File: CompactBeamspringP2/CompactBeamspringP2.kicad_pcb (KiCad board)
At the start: 2 copper layers, 162.3 x 33.2 mm, 54 parts, among them J1 BEAMSPRING CONNECTOR, J3 EXPANSION HEADER, U1 MCP4921-E, U2 LM339A, U3 74AHC595, U4 74AHC595, U5 ProMicro, U7 74AHC595

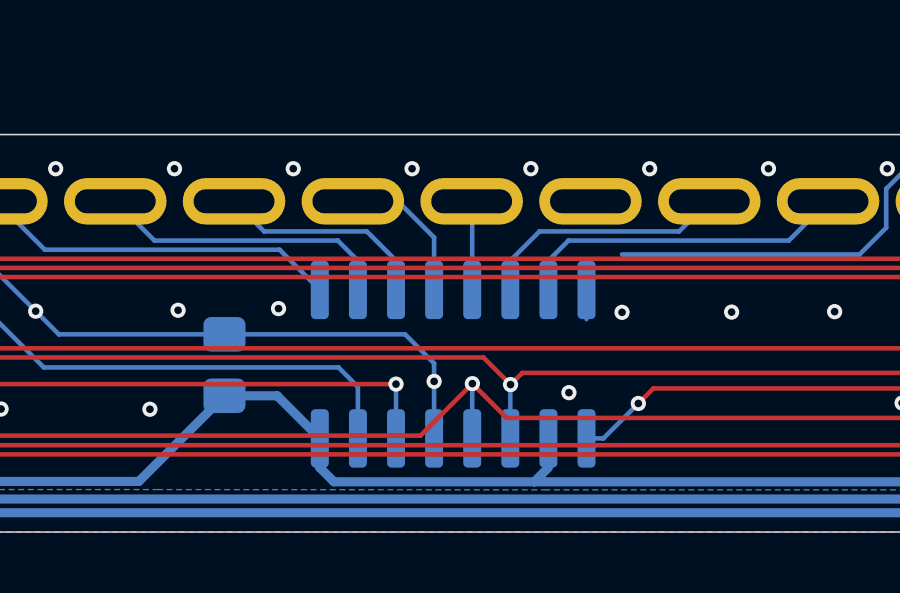
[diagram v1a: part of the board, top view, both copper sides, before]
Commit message: 2-panel: added silkscreen for jlcpcb part number. 1-panel already has it
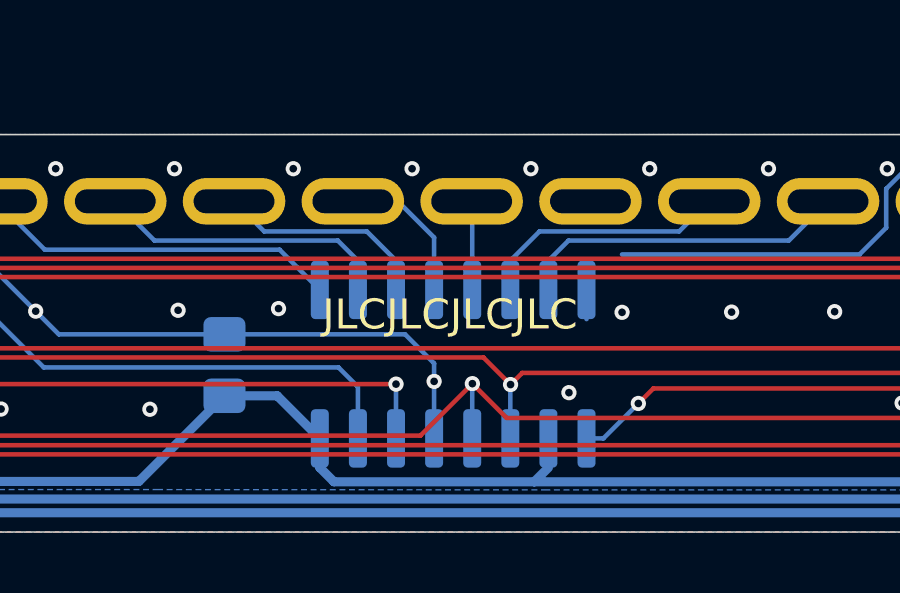
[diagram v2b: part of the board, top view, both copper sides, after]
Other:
- board text added: "JLCJLCJLCJLC"
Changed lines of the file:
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@@
   (general
     (thickness 1.6)
-    (drawings 55)
+    (drawings 56)
     (tracks 1218)
     (zones 0)
@@
     (solder_mask_min_width 0.101)
     (aux_axis_origin 108.7 141.35)
-    (visible_elements 7FFFFF7F)
+    (visible_elements 7FFFF77F)
     (pcbplotparams
       (layerselection 0x010fc_ffffffff)
@@
     )
   )
+  (gr_text JLCJLCJLCJLC (at 198.5 134.1) (layer F.SilkS)
+    (effects (font (size 1 1) (thickness 0.15)))
+  )
   (gr_arc (start 266.75 127.5) (end 266.75 128.1) (angle -180) (layer Edge.Cuts) (width 0.05))

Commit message: More mods
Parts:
- removed the C1 at (238.6, 138.5)
- removed the C1 at (141.0, 111.0)
- removed the C2 at (156.2, 135.8)
- removed the C2 at (223.4, 113.7)
- removed the C3 at (260.5, 135.8)
- removed the C3 at (119.1, 113.7)
- removed the C4 at (191.0, 135.8)
- removed the C4 at (188.7, 113.7)
- removed the C5 at (223.5, 135.8)
- removed the C5 at (156.2, 113.7)
- removed the C6 at (247.3, 133.2)
- removed the C6 at (132.4, 116.3)
- removed the H1 at (269.1, 139.5)
- removed the H1 at (110.5, 110.0)
- removed the J1 at (201.2, 130.3)
- removed the J1 at (178.4, 119.2)
- removed the J3 at (143.4, 127.0)
- removed the J3 at (236.3, 122.5)
- removed the NT1 at (116.4, 135.6)
- removed the NT1 at (263.3, 113.9)
- removed the NT2 at (117.5, 126.5)
- removed the NT2 at (262.2, 123.0)
- removed the R1 at (266.6, 131.1)
- removed the R1 at (113.1, 118.4)
- removed the R2 at (268.9, 131.1)
- removed the R2 at (110.7, 118.4)
- removed the R3 at (246.0, 136.3)
- removed the R3 at (133.7, 113.2)
- removed the R4 at (242.7, 138.5)
- removed the R4 at (137.0, 111.0)
- removed the R5 at (248.4, 136.7)
- removed the R5 at (131.2, 112.8)
- removed the R6 at (138.9, 128.1)
- removed the R6 at (240.7, 121.4)
- removed the R7 at (138.9, 130.1)
- removed the R7 at (240.7, 119.4)
- removed the REF** at (111.2, 136.7)
- removed the REF** at (265.6, 139.6)
- removed the REF** at (268.4, 112.8)
- removed the REF** at (114.1, 109.9)
- removed the RN1 at (262.9, 131.1)
- removed the RN1 at (116.7, 118.4)
- removed the U1 at (240.9, 134.6)
- removed the U1 at (138.8, 114.9)
- removed the U2 at (254.5, 136.2)
- removed the U2 at (125.2, 113.3)
- removed the U3 at (164.3, 135.8)
- removed the U3 at (215.4, 113.7)
- removed the U4 at (198.6, 135.8)
- removed the U4 at (181.0, 113.7)
- removed the U5 at (125.0, 131.9)
- removed the U5 at (254.6, 117.6)
- removed the U7 at (230.6, 135.8)
- removed the U7 at (149.0, 113.7)
- added C1: 0U1, Capacitor_SMD:C_0805_2012Metric_Pad1.15x1.40mm_HandSolder, B.Cu at (232.9, 129.5)
- added C1: 0U1, Capacitor_SMD:C_0805_2012Metric_Pad1.15x1.40mm_HandSolder, B.Cu at (135.3, 101.9)
- added C2: 0U1, Capacitor_SMD:C_0805_2012Metric_Pad1.15x1.40mm_HandSolder, B.Cu at (150.5, 126.7)
- added C2: 0U1, Capacitor_SMD:C_0805_2012Metric_Pad1.15x1.40mm_HandSolder, B.Cu at (217.7, 104.7)
- added C3: 0U1, Capacitor_SMD:C_0805_2012Metric_Pad1.15x1.40mm_HandSolder, B.Cu at (254.8, 126.8)
- added C3: 0U1, Capacitor_SMD:C_0805_2012Metric_Pad1.15x1.40mm_HandSolder, B.Cu at (113.4, 104.6)
- added C4: 0U1, Capacitor_SMD:C_0805_2012Metric_Pad1.15x1.40mm_HandSolder, B.Cu at (185.2, 126.7)
- added C4: 0U1, Capacitor_SMD:C_0805_2012Metric_Pad1.15x1.40mm_HandSolder, B.Cu at (182.9, 104.7)
- added C5: 0U1, Capacitor_SMD:C_0805_2012Metric_Pad1.15x1.40mm_HandSolder, B.Cu at (217.7, 126.7)
- added C5: 0U1, Capacitor_SMD:C_0805_2012Metric_Pad1.15x1.40mm_HandSolder, B.Cu at (150.4, 104.7)
- added C6: 0U1, Capacitor_SMD:C_0805_2012Metric_Pad1.15x1.40mm_HandSolder, B.Cu at (241.5, 124.2)
- added C6: 0U1, Capacitor_SMD:C_0805_2012Metric_Pad1.15x1.40mm_HandSolder, B.Cu at (126.6, 107.2)
- added H1: MountingHole_Pad, TH-XWhatsIt:ChassisGnd, B.Cu at (263.4, 130.4)
- added H1: MountingHole_Pad, TH-XWhatsIt:ChassisGnd, B.Cu at (104.8, 101.0)
- added J1: BEAMSPRING CONNECTOR, TH-XWhatsIt:30-pin-universal-beamspring-connector_v2, F.Cu at (195.5, 121.3)
- added J1: BEAMSPRING CONNECTOR, TH-XWhatsIt:30-pin-universal-beamspring-connector_v2, F.Cu at (172.7, 110.1)
- added J2: PadsToShort, TH-XWhatsIt:PadsToShort, B.Cu at (109.0, 118.5)
- added J2: PadsToShort, TH-XWhatsIt:PadsToShort, B.Cu at (259.1, 112.9)
- added J3: EXPANSION HEADER, Connector_PinHeader_2.54mm:PinHeader_2x03_P2.54mm_Vertical, F.Cu at (137.6, 117.9)
- added J3: EXPANSION HEADER, Connector_PinHeader_2.54mm:PinHeader_2x03_P2.54mm_Vertical, F.Cu at (230.5, 113.5)
- added NT1: Net-Tie_3, NetTie:NetTie-3_THT_Pad0.3mm, B.Cu at (110.6, 126.5)
- added NT1: Net-Tie_3, NetTie:NetTie-3_THT_Pad0.3mm, B.Cu at (257.5, 104.9)
- added NT2: Net-Tie_3, NetTie:NetTie-3_THT_Pad0.3mm, B.Cu at (111.7, 117.4)
- added NT2: Net-Tie_3, NetTie:NetTie-3_THT_Pad0.3mm, B.Cu at (256.4, 114.0)
- added R1: 4K7, Resistor_SMD:R_0805_2012Metric_Pad1.15x1.40mm_HandSolder, B.Cu at (260.8, 122.0)
- added R1: 4K7, Resistor_SMD:R_0805_2012Metric_Pad1.15x1.40mm_HandSolder, B.Cu at (107.3, 109.4)
- added R2: 1K, Resistor_SMD:R_0805_2012Metric_Pad1.15x1.40mm_HandSolder, B.Cu at (263.2, 122.0)
- added R2: 1K, Resistor_SMD:R_0805_2012Metric_Pad1.15x1.40mm_HandSolder, B.Cu at (105.0, 109.4)
- added R3: 20K, Resistor_SMD:R_0805_2012Metric_Pad1.15x1.40mm_HandSolder, B.Cu at (240.2, 127.2)
- added R3: 20K, Resistor_SMD:R_0805_2012Metric_Pad1.15x1.40mm_HandSolder, B.Cu at (127.9, 104.2)
- added R4: 20K, Resistor_SMD:R_0805_2012Metric_Pad1.15x1.40mm_HandSolder, B.Cu at (236.9, 129.5)
- added R4: 20K, Resistor_SMD:R_0805_2012Metric_Pad1.15x1.40mm_HandSolder, B.Cu at (131.2, 101.9)
- added R5: 4K7, Resistor_SMD:R_0805_2012Metric_Pad1.15x1.40mm_HandSolder, B.Cu at (242.7, 127.6)
- added R5: 4K7, Resistor_SMD:R_0805_2012Metric_Pad1.15x1.40mm_HandSolder, B.Cu at (125.5, 103.8)
- added R6: Not Mounted, Resistor_SMD:R_0805_2012Metric_Pad1.15x1.40mm_HandSolder, B.Cu at (132.3, 119.0)
- added R6: Not Mounted, Resistor_SMD:R_0805_2012Metric_Pad1.15x1.40mm_HandSolder, B.Cu at (235.8, 112.4)
- added R7: Not Mounted, Resistor_SMD:R_0805_2012Metric_Pad1.15x1.40mm_HandSolder, B.Cu at (132.3, 121.0)
- added R7: Not Mounted, Resistor_SMD:R_0805_2012Metric_Pad1.15x1.40mm_HandSolder, B.Cu at (235.8, 110.4)
- added R8: Not Mounted, Resistor_SMD:R_0805_2012Metric_Pad1.15x1.40mm_HandSolder, B.Cu at (132.3, 123.0)
- added R8: Not Mounted, Resistor_SMD:R_0805_2012Metric_Pad1.15x1.40mm_HandSolder, B.Cu at (235.8, 108.4)
- added REF**: tooling_hole, TH-XWhatsIt:tooling_hole, F.Cu at (105.5, 127.6)
- added REF**: tooling_hole, TH-XWhatsIt:tooling_hole, F.Cu at (259.8, 130.6)
- added REF**: tooling_hole, TH-XWhatsIt:tooling_hole, F.Cu at (262.7, 103.8)
- added REF**: tooling_hole, TH-XWhatsIt:tooling_hole, F.Cu at (108.3, 100.8)
- added RN1: 100K, Resistor_SMD:R_Array_Convex_4x0603, B.Cu at (257.2, 122.1)
- added RN1: 100K, Resistor_SMD:R_Array_Convex_4x0603, B.Cu at (111.0, 109.3)
- added TP1: Dac Output, TestPoint:TestPoint_Pad_D1.0mm, B.Cu at (240.9, 131.1)
- added TP1: Dac Output, TestPoint:TestPoint_Pad_D1.0mm, B.Cu at (127.2, 100.3)
- added TP2: Threshold Voltage, TestPoint:TestPoint_Pad_D1.0mm, B.Cu at (256.8, 129.9)
- added TP2: Threshold Voltage, TestPoint:TestPoint_Pad_D1.0mm, B.Cu at (111.3, 101.5)
- added U1: MCP4921-E, Package_SO:SOIC-8_3.9x4.9mm_P1.27mm, B.Cu at (235.1, 125.6)
- added U1: MCP4921-E, Package_SO:SOIC-8_3.9x4.9mm_P1.27mm, B.Cu at (133.0, 105.8)
- added U2: LM339A, Package_SO:SOIC-14_3.9x8.7mm_P1.27mm, B.Cu at (248.7, 127.1)
- added U2: LM339A, Package_SO:SOIC-14_3.9x8.7mm_P1.27mm, B.Cu at (119.4, 104.3)
- added U3: 74AHC595, Package_SO:SOIC-16_3.9x9.9mm_P1.27mm, B.Cu at (158.5, 126.7)
- added U3: 74AHC595, Package_SO:SOIC-16_3.9x9.9mm_P1.27mm, B.Cu at (209.6, 104.7)
- added U4: 74AHC595, Package_SO:SOIC-16_3.9x9.9mm_P1.27mm, B.Cu at (192.9, 126.7)
- added U4: 74AHC595, Package_SO:SOIC-16_3.9x9.9mm_P1.27mm, B.Cu at (175.3, 104.7)
- added U5: ProMicro, promicro:ProMicro, F.Cu at (119.3, 122.8)
- added U5: ProMicro, promicro:ProMicro, F.Cu at (248.9, 108.6)
- added U7: 74AHC595, Package_SO:SOIC-16_3.9x9.9mm_P1.27mm, B.Cu at (224.9, 126.7)
- added U7: 74AHC595, Package_SO:SOIC-16_3.9x9.9mm_P1.27mm, B.Cu at (143.3, 104.7)
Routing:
- net HEADER3: track 41.2 -> 89.9 mm
- net GNDD: track 267.9 -> 221.8 mm, vias 126 -> 146
- net GND: track 0.00 -> 44.3 mm
- net Net-(NT1-Pad2): track 42.9 -> 0.00 mm
- net GNDA: track 305.2 -> 262.6 mm, vias 52 -> 64
- net HEADER4: track 51.4 -> 87.2 mm
- net Net-(R8-Pad1): track 0.00 -> 30.3 mm
- net ROW1: track 239.3 -> 265.6 mm
- net HEADER2: track 90.4 -> 66.9 mm, vias 0 -> 4
- net +5VD: track 296.1 -> 317.2 mm
- net HEADER1: track 108.4 -> 87.8 mm, vias 0 -> 4
- net +5VA: track 373.7 -> 393.7 mm, vias 0 -> 4
- net ROW3: track 236.3 -> 255.7 mm
- net RST: track 0.00 -> 12.7 mm
- net Net-(R4-Pad2): track 5.33 -> 18.0 mm
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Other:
- outline, holes or cut-outs redrawn
- board text added: "Compact-Beamspring Rev1.2"
- board text added: "DAC"
- board text added: "Threshold"
- board text added: "Voltage"
- board text added: "Vout"
- board text removed: "Compact-Beamspring Rev1.1"
- board text removed: "JLCJLCJLCJLC"

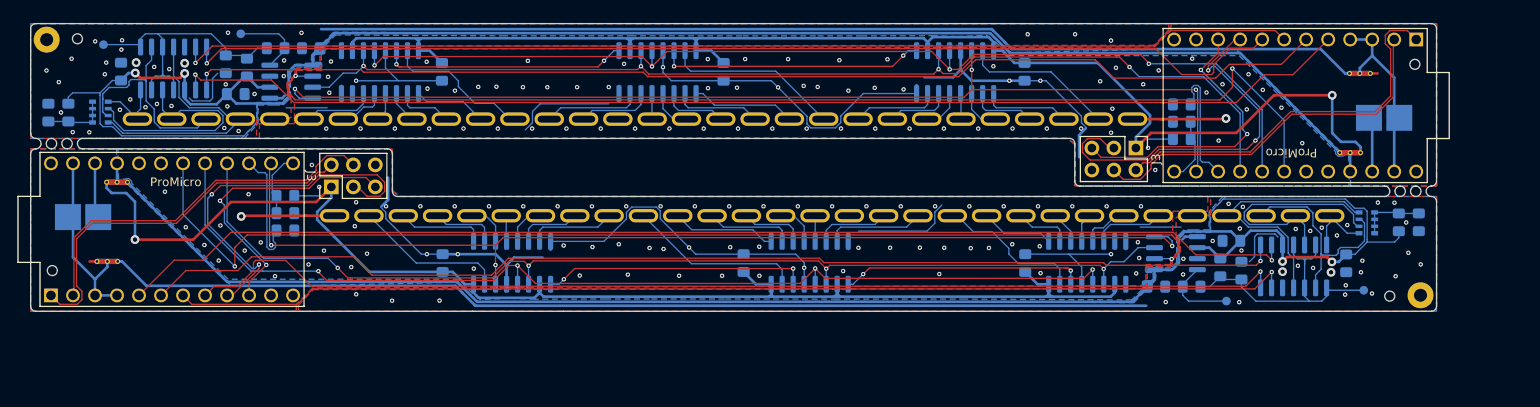
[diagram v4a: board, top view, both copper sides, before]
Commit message: Moved to individual resistors instead of resistor network, added a bit more space next to the promicro
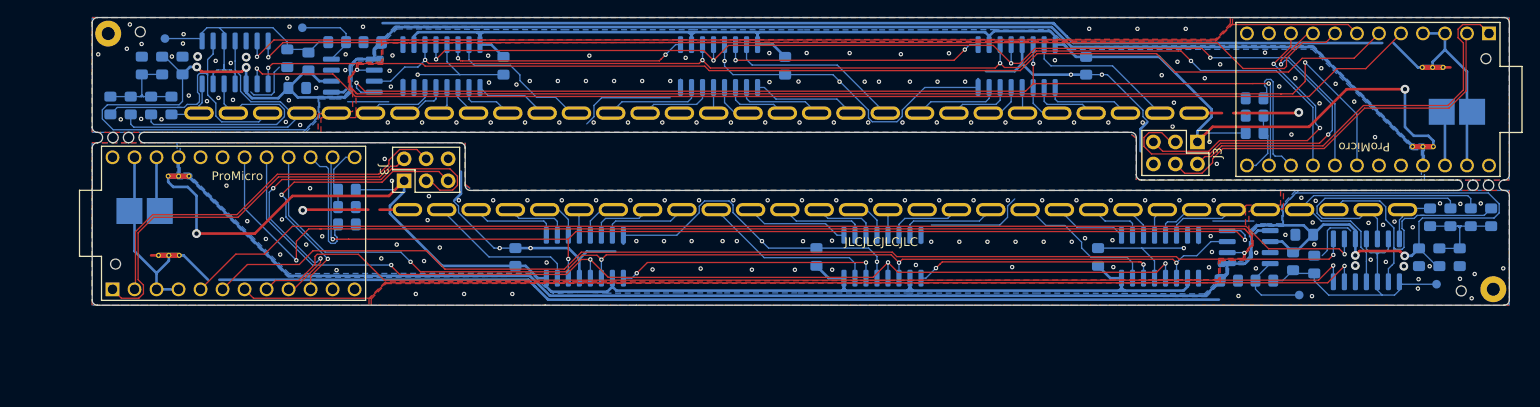
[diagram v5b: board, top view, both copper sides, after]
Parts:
- removed the C1 at (232.9, 129.5)
- removed the C1 at (135.3, 101.9)
- removed the C2 at (150.5, 126.7)
- removed the C2 at (217.7, 104.7)
- removed the C3 at (254.8, 126.8)
- removed the C3 at (113.4, 104.6)
- removed the C4 at (185.2, 126.7)
- removed the C4 at (182.9, 104.7)
- removed the C5 at (217.7, 126.7)
- removed the C5 at (150.4, 104.7)
- removed the C6 at (241.5, 124.2)
- removed the C6 at (126.6, 107.2)
- removed the H1 at (263.4, 130.4)
- removed the H1 at (104.8, 101.0)
- removed the J1 at (195.5, 121.3)
- removed the J1 at (172.7, 110.1)
- removed the J2 at (109.0, 118.5)
- removed the J2 at (259.1, 112.9)
- removed the J3 at (137.6, 117.9)
- removed the J3 at (230.5, 113.5)
- removed the NT1 at (110.6, 126.5)
- removed the NT1 at (257.5, 104.9)
- removed the NT2 at (111.7, 117.4)
- removed the NT2 at (256.4, 114.0)
- removed the R1 at (260.8, 122.0)
- removed the R1 at (107.3, 109.4)
- removed the R2 at (263.2, 122.0)
- removed the R2 at (105.0, 109.4)
- removed the R3 at (240.2, 127.2)
- removed the R3 at (127.9, 104.2)
- removed the R4 at (236.9, 129.5)
- removed the R4 at (131.2, 101.9)
- removed the R5 at (242.7, 127.6)
- removed the R5 at (125.5, 103.8)
- removed the R6 at (132.3, 119.0)
- removed the R6 at (235.8, 112.4)
- removed the R7 at (132.3, 121.0)
- removed the R7 at (235.8, 110.4)
- removed the R8 at (132.3, 123.0)
- removed the R8 at (235.8, 108.4)
- removed the REF** at (105.5, 127.6)
- removed the REF** at (259.8, 130.6)
- removed the REF** at (262.7, 103.8)
- removed the REF** at (108.3, 100.8)
- removed RN1 (x2): 100K, Resistor_SMD:R_Array_Convex_4x0603
- removed the TP1 at (240.9, 131.1)
- removed the TP1 at (127.2, 100.3)
- removed the TP2 at (256.8, 129.9)
- removed the TP2 at (111.3, 101.5)
- removed the U1 at (235.1, 125.6)
- removed the U1 at (133.0, 105.8)
- removed the U2 at (248.7, 127.1)
- removed the U2 at (119.4, 104.3)
- removed the U3 at (158.5, 126.7)
- removed the U3 at (209.6, 104.7)
- removed the U4 at (192.9, 126.7)
- removed the U4 at (175.3, 104.7)
- removed the U5 at (119.3, 122.8)
- removed the U5 at (248.9, 108.6)
- removed the U7 at (224.9, 126.7)
- removed the U7 at (143.3, 104.7)
- added C1: 0U1, Capacitor_SMD:C_0805_2012Metric_Pad1.15x1.40mm_HandSolder, B.Cu at (241.3, 128.8)
- added C1: 0U1, Capacitor_SMD:C_0805_2012Metric_Pad1.15x1.40mm_HandSolder, B.Cu at (142.4, 101.2)
- added C2: 0U1, Capacitor_SMD:C_0805_2012Metric_Pad1.15x1.40mm_HandSolder, B.Cu at (158.9, 126.0)
- added C2: 0U1, Capacitor_SMD:C_0805_2012Metric_Pad1.15x1.40mm_HandSolder, B.Cu at (224.8, 104.0)
- added C3: 0U1, Capacitor_SMD:C_0805_2012Metric_Pad1.15x1.40mm_HandSolder, B.Cu at (263.2, 126.1)
- added C3: 0U1, Capacitor_SMD:C_0805_2012Metric_Pad1.15x1.40mm_HandSolder, B.Cu at (120.5, 103.9)
- added C4: 0U1, Capacitor_SMD:C_0805_2012Metric_Pad1.15x1.40mm_HandSolder, B.Cu at (193.6, 126.0)
- added C4: 0U1, Capacitor_SMD:C_0805_2012Metric_Pad1.15x1.40mm_HandSolder, B.Cu at (190.0, 104.0)
- added C5: 0U1, Capacitor_SMD:C_0805_2012Metric_Pad1.15x1.40mm_HandSolder, B.Cu at (226.1, 126.0)
- added C5: 0U1, Capacitor_SMD:C_0805_2012Metric_Pad1.15x1.40mm_HandSolder, B.Cu at (157.5, 104.0)
- added C6: 0U1, Capacitor_SMD:C_0805_2012Metric_Pad1.15x1.40mm_HandSolder, B.Cu at (249.9, 123.5)
- added C6: 0U1, Capacitor_SMD:C_0805_2012Metric_Pad1.15x1.40mm_HandSolder, B.Cu at (133.7, 106.5)
- added H1: MountingHole_Pad, TH-XWhatsIt:ChassisGnd, B.Cu at (271.8, 129.8)
- added H1: MountingHole_Pad, TH-XWhatsIt:ChassisGnd, B.Cu at (111.9, 100.2)
- added J1: BEAMSPRING CONNECTOR, TH-XWhatsIt:30-pin-universal-beamspring-connector_v2, F.Cu at (203.9, 120.6)
- added J1: BEAMSPRING CONNECTOR, TH-XWhatsIt:30-pin-universal-beamspring-connector_v2, F.Cu at (179.8, 109.4)
- added J2: PadsToShort, TH-XWhatsIt:PadsToShort, B.Cu at (116.1, 117.8)
- added J2: PadsToShort, TH-XWhatsIt:PadsToShort, B.Cu at (267.6, 112.2)
- added J3: EXPANSION HEADER, Connector_PinHeader_2.54mm:PinHeader_2x03_P2.54mm_Vertical, F.Cu at (146.0, 117.2)
- added J3: EXPANSION HEADER, Connector_PinHeader_2.54mm:PinHeader_2x03_P2.54mm_Vertical, F.Cu at (237.6, 112.8)
- added NT1: Net-Tie_3, NetTie:NetTie-3_THT_Pad0.3mm, B.Cu at (117.7, 125.8)
- added NT1: Net-Tie_3, NetTie:NetTie-3_THT_Pad0.3mm, B.Cu at (265.9, 104.2)
- added NT2: Net-Tie_3, NetTie:NetTie-3_THT_Pad0.3mm, B.Cu at (118.8, 116.7)
- added NT2: Net-Tie_3, NetTie:NetTie-3_THT_Pad0.3mm, B.Cu at (264.8, 113.3)
- added R1: 4K7, Resistor_SMD:R_0805_2012Metric_Pad1.15x1.40mm_HandSolder, B.Cu at (265.5, 126.1)
- added R1: 4K7, Resistor_SMD:R_0805_2012Metric_Pad1.15x1.40mm_HandSolder, B.Cu at (118.1, 103.9)
- added R10: 100k 1%, Resistor_SMD:R_0805_2012Metric_Pad1.15x1.40mm_HandSolder, B.Cu at (264.4, 121.5)
- added R10: 100k 1%, Resistor_SMD:R_0805_2012Metric_Pad1.15x1.40mm_HandSolder, B.Cu at (119.2, 108.5)
- added R11: 100k 1%, Resistor_SMD:R_0805_2012Metric_Pad1.15x1.40mm_HandSolder, B.Cu at (269.1, 121.5)
- added R11: 100k 1%, Resistor_SMD:R_0805_2012Metric_Pad1.15x1.40mm_HandSolder, B.Cu at (114.5, 108.5)
- added R12: 100k 1%, Resistor_SMD:R_0805_2012Metric_Pad1.15x1.40mm_HandSolder, B.Cu at (271.5, 121.5)
- added R12: 100k 1%, Resistor_SMD:R_0805_2012Metric_Pad1.15x1.40mm_HandSolder, B.Cu at (112.2, 108.5)
- added R2: 1K, Resistor_SMD:R_0805_2012Metric_Pad1.15x1.40mm_HandSolder, B.Cu at (267.9, 126.1)
- added R2: 1K, Resistor_SMD:R_0805_2012Metric_Pad1.15x1.40mm_HandSolder, B.Cu at (115.8, 103.9)
- added R3: 20K, Resistor_SMD:R_0805_2012Metric_Pad1.15x1.40mm_HandSolder, B.Cu at (248.6, 126.5)
- added R3: 20K, Resistor_SMD:R_0805_2012Metric_Pad1.15x1.40mm_HandSolder, B.Cu at (135.0, 103.5)
- added R4: 20K, Resistor_SMD:R_0805_2012Metric_Pad1.15x1.40mm_HandSolder, B.Cu at (245.3, 128.8)
- added R4: 20K, Resistor_SMD:R_0805_2012Metric_Pad1.15x1.40mm_HandSolder, B.Cu at (138.3, 101.2)
- added R5: 4K7, Resistor_SMD:R_0805_2012Metric_Pad1.15x1.40mm_HandSolder, B.Cu at (251.1, 126.9)
- added R5: 4K7, Resistor_SMD:R_0805_2012Metric_Pad1.15x1.40mm_HandSolder, B.Cu at (132.6, 103.1)
- added R6: Not Mounted, Resistor_SMD:R_0805_2012Metric_Pad1.15x1.40mm_HandSolder, B.Cu at (139.4, 118.3)
- added R6: Not Mounted, Resistor_SMD:R_0805_2012Metric_Pad1.15x1.40mm_HandSolder, B.Cu at (244.2, 111.7)
- added R7: Not Mounted, Resistor_SMD:R_0805_2012Metric_Pad1.15x1.40mm_HandSolder, B.Cu at (139.4, 120.3)
- added R7: Not Mounted, Resistor_SMD:R_0805_2012Metric_Pad1.15x1.40mm_HandSolder, B.Cu at (244.2, 109.7)
- added R8: Not Mounted, Resistor_SMD:R_0805_2012Metric_Pad1.15x1.40mm_HandSolder, B.Cu at (139.4, 122.3)
- added R8: Not Mounted, Resistor_SMD:R_0805_2012Metric_Pad1.15x1.40mm_HandSolder, B.Cu at (244.2, 107.7)
- added R9: 100k 1%, Resistor_SMD:R_0805_2012Metric_Pad1.15x1.40mm_HandSolder, B.Cu at (266.8, 121.5)
- added R9: 100k 1%, Resistor_SMD:R_0805_2012Metric_Pad1.15x1.40mm_HandSolder, B.Cu at (116.8, 108.5)
- added REF**: tooling_hole, TH-XWhatsIt:tooling_hole, F.Cu at (112.8, 126.8)
- added REF**: tooling_hole, TH-XWhatsIt:tooling_hole, F.Cu at (268.1, 129.9)
- added REF**: tooling_hole, TH-XWhatsIt:tooling_hole, F.Cu at (270.9, 103.2)
- added REF**: tooling_hole, TH-XWhatsIt:tooling_hole, F.Cu at (115.6, 100.0)
- added TP1: Dac Output, TestPoint:TestPoint_Pad_D1.0mm, B.Cu at (249.3, 130.4)
- added TP1: Dac Output, TestPoint:TestPoint_Pad_D1.0mm, B.Cu at (134.3, 99.6)
- added TP2: Threshold Voltage, TestPoint:TestPoint_Pad_D1.0mm, B.Cu at (265.2, 129.2)
- added TP2: Threshold Voltage, TestPoint:TestPoint_Pad_D1.0mm, B.Cu at (118.5, 100.8)
- added U1: MCP4921-E, Package_SO:SOIC-8_3.9x4.9mm_P1.27mm, B.Cu at (243.5, 124.9)
- added U1: MCP4921-E, Package_SO:SOIC-8_3.9x4.9mm_P1.27mm, B.Cu at (140.1, 105.1)
- added U2: LM339A, Package_SO:SOIC-14_3.9x8.7mm_P1.27mm, B.Cu at (257.1, 126.4)
- added U2: LM339A, Package_SO:SOIC-14_3.9x8.7mm_P1.27mm, B.Cu at (126.5, 103.6)
- added U3: 74AHC595, Package_SO:SOIC-16_3.9x9.9mm_P1.27mm, B.Cu at (166.9, 126.0)
- added U3: 74AHC595, Package_SO:SOIC-16_3.9x9.9mm_P1.27mm, B.Cu at (216.7, 104.0)
- added U4: 74AHC595, Package_SO:SOIC-16_3.9x9.9mm_P1.27mm, B.Cu at (201.3, 126.0)
- added U4: 74AHC595, Package_SO:SOIC-16_3.9x9.9mm_P1.27mm, B.Cu at (182.4, 104.0)
- added U5: ProMicro, promicro:ProMicro, F.Cu at (126.4, 122.1)
- added U5: ProMicro, promicro:ProMicro, F.Cu at (257.3, 107.9)
- added U7: 74AHC595, Package_SO:SOIC-16_3.9x9.9mm_P1.27mm, B.Cu at (233.3, 126.0)
- added U7: 74AHC595, Package_SO:SOIC-16_3.9x9.9mm_P1.27mm, B.Cu at (150.4, 104.0)
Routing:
- net +5VA: track 393.7 -> 421.2 mm
- net SENSE3: track 52.1 -> 64.1 mm
- net SENSE4: track 61.3 -> 71.8 mm
- net BIAS: track 15.1 -> 25.0 mm
- net +5VD: track 317.2 -> 322.4 mm
- net SENSE2: track 52.8 -> 55.9 mm
- net ~SELECTDAC: track 261.6 -> 264.4 mm
- net MOSI: track 245.4 -> 248.0 mm
- net CLOCK: track 250.4 -> 253.0 mm
- net ROW4: track 258.9 -> 261.5 mm
- net HEADER3: track 89.9 -> 92.5 mm
- net HEADER1: track 87.8 -> 90.4 mm
- net LOADCOL: track 242.3 -> 244.9 mm
- net HEADER4: track 87.2 -> 89.8 mm
- net ROW3: track 255.7 -> 258.3 mm
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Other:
- board size 162.3 x 33.2 mm -> 163.6 x 33.2 mm
- board text added: "Compact-Beamspring Rev1.3"
- board text added: "JLCJLCJLCJLC"
- board text removed: "Compact-Beamspring Rev1.2"
